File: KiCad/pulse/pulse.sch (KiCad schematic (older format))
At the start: 15 parts, among them K2 ISP, P1 LAMP, P2 12V, P3 ND, Q1 2N7000, U1 ATTINY45/V

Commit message: pulse - final gerber files created. BoM finalized
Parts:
- added PB3: ND, Pad01, symbol CONN_1
- D1, D2: footprint d_0805 -> SOD323F
- D3: footprint (none) -> SOD523F
- U1: value ATTINY45/V -> ATTINY45-20SU
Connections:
- net ADC3: now also PB3.1
- no-connect marks 1 -> 0
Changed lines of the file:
@@
-EESchema Schematic File Version 2  date 6/21/2012 12:13:16 PM
+EESchema Schematic File Version 2  date 6/21/2012 4:50:03 PM
 LIBS:power
 LIBS:pulse
@@
 Sheet 1 1
 Title "Throbber - Bike Neutral Indicator"
-Date "20 jun 2012"
+Date "21 jun 2012"
 Rev "A"
 Comp "WyoLum"
@@
 $EndDescr
 Wire Wire Line
-	2250 2250 1950 2250
-Connection ~ 3400 4400
-Wire Wire Line
-	3050 4400 8650 4400
-Wire Wire Line
-	3050 4400 3050 2450
-Connection ~ 7200 4400
-Connection ~ 3700 4400
-Connection ~ 5150 4400
-Wire Wire Line
-	1950 1850 8650 1850
-Wire Wire Line
-	3050 2450 1950 2450
+	4700 3150 4700 3000
+Wire Wire Line
+	5400 3150 4700 3150
+Connection ~ 3050 2250
+Wire Wire Line
+	2650 2250 4150 2250
+Connection ~ 5350 4400
+Wire Wire Line
+	3050 2250 3050 1650
+Wire Wire Line
+	3050 1650 1950 1650
+Wire Wire Line
+	3400 4400 3400 4150
+Connection ~ 7200 2250
+Wire Wire Line
+	7200 3700 7200 2200
+Wire Wire Line
+	2450 7450 2850 7450
+Wire Wire Line
+	2450 7250 2850 7250
+Wire Wire Line
+	2450 7050 2850 7050
+Wire Wire Line
+	5400 3050 4900 3050
+Connection ~ 5150 3250
+Wire Wire Line
+	7000 3350 7650 3350
+Wire Wire Line
+	7000 3150 7400 3150
+Wire Wire Line
+	8650 2750 8650 1850
+Connection ~ 7200 3600
+Wire Wire Line
+	7500 3700 7500 3600
+Wire Wire Line
+	7500 3600 7200 3600
+Wire Wire Line
+	7200 4100 7200 4400
+Wire Wire Line
+	8150 3350 8200 3350
+Connection ~ 5150 4200
+Wire Wire Line
+	5150 4400 5150 4100
+Wire Wire Line
+	5400 3350 5350 3350
+Connection ~ 5150 3600
+Wire Wire Line
+	5150 3600 4900 3600
+Wire Wire Line
+	4900 3600 4900 3700
+Wire Wire Line
+	4650 3250 5400 3250
+Wire Wire Line
+	5150 3250 5150 3700
+Wire Wire Line
+	4900 4100 4900 4200
+Wire Wire Line
+	4900 4200 5150 4200
+Wire Wire Line
+	5350 3350 5350 4400
+Wire Wire Line
+	4650 2250 7200 2250
+Wire Wire Line
+	7200 4200 7500 4200
+Wire Wire Line
+	7500 4200 7500 4100
+Connection ~ 7200 4200
+Wire Wire Line
+	7200 3050 7000 3050
+Connection ~ 7200 3050
+Wire Wire Line
+	3700 4400 3700 4500
+Wire Wire Line
+	8650 3650 8650 4400
+Wire Wire Line
+	7000 3250 7400 3250
+Wire Wire Line
+	4150 3250 1950 3250
+Wire Wire Line
+	2850 6950 2450 6950
+Wire Wire Line
+	2850 7150 2450 7150
+Wire Wire Line
+	2850 7350 2450 7350
+Wire Notes Line
+	2150 7550 3350 7550
+Wire Notes Line
+	2150 7550 2150 6650
+Wire Notes Line
+	2150 6650 3350 6650
 Wire Notes Line
 	3350 6650 3350 7550
-Wire Notes Line
-	3350 6650 2150 6650
-Wire Notes Line
-	2150 6650 2150 7550
-Wire Notes Line
-	2150 7550 3350 7550
-Wire Wire Line
-	2850 7350 2450 7350
-Wire Wire Line
-	2850 7150 2450 7150
-Wire Wire Line
-	2850 6950 2450 6950
-Wire Wire Line
-	4150 3250 1950 3250
-Wire Wire Line
-	5400 3150 4900 3150
-Wire Wire Line
-	7000 3250 7400 3250
-Wire Wire Line
-	8650 4400 8650 3650
-Wire Wire Line
-	3700 4400 3700 4500
-Connection ~ 7200 3050
-Wire Wire Line
-	7200 3050 7000 3050
-Connection ~ 7200 4200
-Wire Wire Line
-	7500 4100 7500 4200
-Wire Wire Line
-	7500 4200 7200 4200
-Wire Wire Line
-	4650 2250 7200 2250
-Wire Wire Line
-	5350 4400 5350 3350
-Wire Wire Line
-	5150 4200 4900 4200
-Wire Wire Line
-	4900 4200 4900 4100
-Wire Wire Line
-	5150 3250 5150 3700
-Wire Wire Line
-	4650 3250 5400 3250
-Wire Wire Line
-	4900 3700 4900 3600
-Wire Wire Line
-	4900 3600 5150 3600
-Connection ~ 5150 3600
-Wire Wire Line
-	5350 3350 5400 3350
-Wire Wire Line
-	5150 4400 5150 4100
-Connection ~ 5150 4200
-Wire Wire Line
-	8150 3350 8200 3350
-Wire Wire Line
-	7200 4100 7200 4400
-Wire Wire Line
-	7200 3600 7500 3600
-Wire Wire Line
-	7500 3600 7500 3700
-Connection ~ 7200 3600
-Wire Wire Line
-	8650 1850 8650 2750
-Wire Wire Line
-	7000 3150 7400 3150
-Wire Wire Line
-	7000 3350 7650 3350
-Connection ~ 5150 3250
-Wire Wire Line
-	5400 3050 4900 3050
-Wire Wire Line
-	2450 7050 2850 7050
-Wire Wire Line
-	2450 7250 2850 7250
-Wire Wire Line
-	2450 7450 2850 7450
-Wire Wire Line
-	7200 3700 7200 2200
-Connection ~ 7200 2250
-Wire Wire Line
-	3400 4400 3400 4150
-Wire Wire Line
-	1950 1650 3050 1650
-Wire Wire Line
-	3050 1650 3050 2250
-Connection ~ 5350 4400
-Wire Wire Line
-	2650 2250 4150 2250
-Connection ~ 3050 2250
+Wire Wire Line
+	1950 2450 3050 2450
+Wire Wire Line
+	8650 1850 1950 1850
+Connection ~ 5150 4400
+Connection ~ 3700 4400
+Connection ~ 7200 4400
+Wire Wire Line
+	3050 2450 3050 4400
+Wire Wire Line
+	3050 4400 8650 4400
+Connection ~ 3400 4400
+Wire Wire Line
+	2250 2250 1950 2250
+$Comp
+L CONN_1 PB3
+U 1 1 4FE302FC
+P 4700 2850
+F 0 "PB3" V 4775 2825 40  0000 L CNN
+F 1 "ND" H 4700 2905 30  0001 C CNN
+F 2 "Pad01" H 4700 3005 30  0001 C CNN
+	1    4700 2850
+	0    -1   -1   0
+$EndComp
 $Comp
 L DIODE D3
@@
 F 0 "D3" H 2450 2350 40  0000 C CNN
 F 1 "1N4448WT" H 2450 2150 40  0000 C CNN
+F 2 "SOD523F" H 2450 2250 40  0001 C CNN
 	1    2450 2250
 	1    0    0    -1
@@
 	-1   0    0    -1
 $EndComp
-NoConn ~ 4900 3150
 $Comp
 L PWR_FLAG #FLG1
@@
 U 1 1 4FE071E3
 P 8500 3200
-F 0 "Q1" H 8250 3400 60  0000 C CNN
-F 1 "2N7000" H 8100 3250 60  0000 C CNN
+F 0 "Q1" H 8250 3450 60  0000 C CNN
+F 1 "2N7000" H 8150 3350 60  0000 C CNN
 F 2 "SOT23-3" H 8100 3350 60  0001 C CNN
+F 3 "SSM3K7002BF" H 8050 3250 50  0000 C CNN
 	1    8500 3200
 	1    0    0    -1
@@
 P 6200 3200
 F 0 "U1" H 5600 3500 50  0000 L BNN
-F 1 "ATTINY45/V" H 5600 2850 50  0000 L BNN
+F 1 "ATTINY45-20SU" H 5600 2850 50  0000 L BNN
 F 2 "SO8E" H 6700 2775 50  0001 C CNN
 	1    6200 3200
@@
 F 0 "D2" H 7300 3850 40  0000 C CNN
 F 1 "Z5V1" H 7200 3775 40  0000 C CNN
-F 2 "d_0805" H 7200 3900 60  0001 C CNN
+F 2 "SOD323F" H 7200 3900 60  0001 C CNN
+F 3 "MM3Z5V1C" H 7200 4000 50  0000 C CNN
 	1    7200 3900
 	0    -1   -1   0
@@
 F 0 "D1" H 5250 3850 40  0000 C CNN
 F 1 "Z5V1" H 5150 3775 40  0000 C CNN
-F 2 "d_0805" H 5150 3900 60  0001 C CNN
+F 2 "SOD323F" H 5150 3900 60  0001 C CNN
+F 3 "MM3Z5V1C" H 5150 3650 50  0000 C CNN
 	1    5150 3900
 	0    -1   -1   0

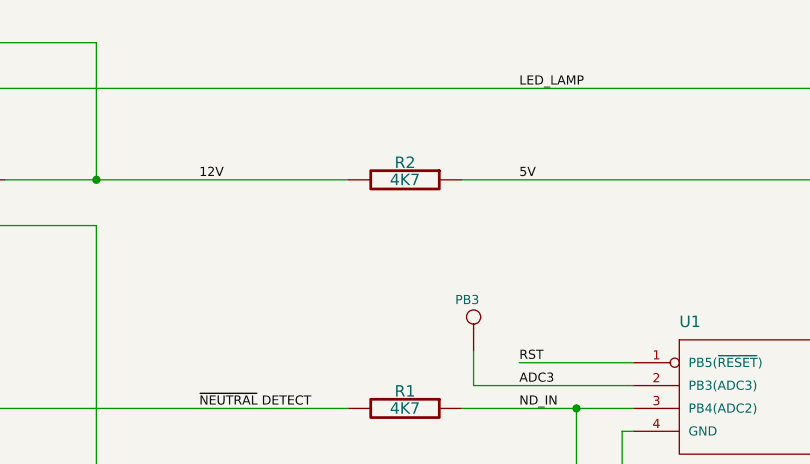
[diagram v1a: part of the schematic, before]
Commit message: p.u.l.s.e. some changes based on initial testing - need higher wattage for series dropping resistor - since avg. Batt voltage = 14V
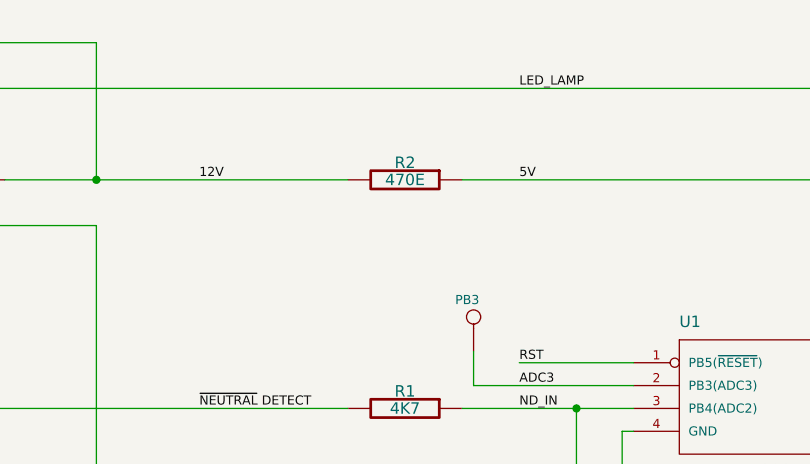
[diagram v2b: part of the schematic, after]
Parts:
- R2: value 4K7 -> 470E
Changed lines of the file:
@@
-EESchema Schematic File Version 2  date 6/21/2012 4:50:03 PM
+EESchema Schematic File Version 2  date 7/21/2012 10:30:47 AM
 LIBS:power
 LIBS:pulse
@@
 Sheet 1 1
 Title "Throbber - Bike Neutral Indicator"
-Date "21 jun 2012"
+Date "21 jul 2012"
 Rev "A"
 Comp "WyoLum"
@@
 P 4400 2250
 F 0 "R2" V 4325 2250 50  0000 C CNN
-F 1 "4K7" V 4400 2250 50  0000 C CNN
+F 1 "470E" V 4400 2250 50  0000 C CNN
 F 2 "r_0805" H 4400 2250 60  0001 C CNN
 	1    4400 2250
